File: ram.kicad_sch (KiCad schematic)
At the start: 9 parts, among them U10 HyperRAM

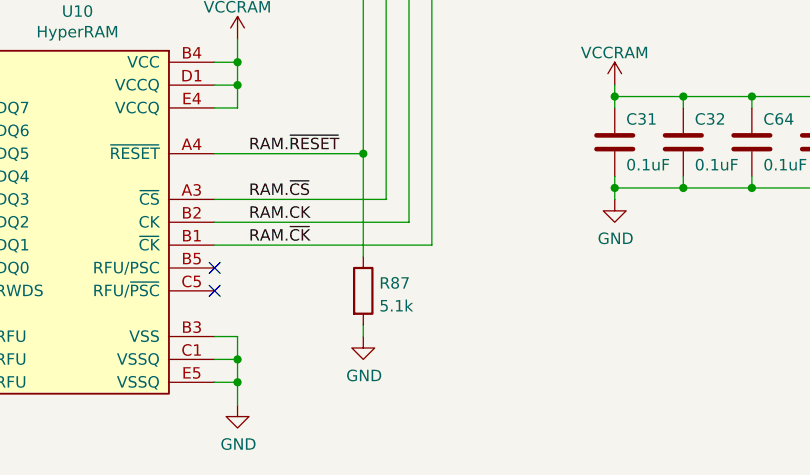
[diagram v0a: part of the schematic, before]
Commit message: add first round of hits on lcsc
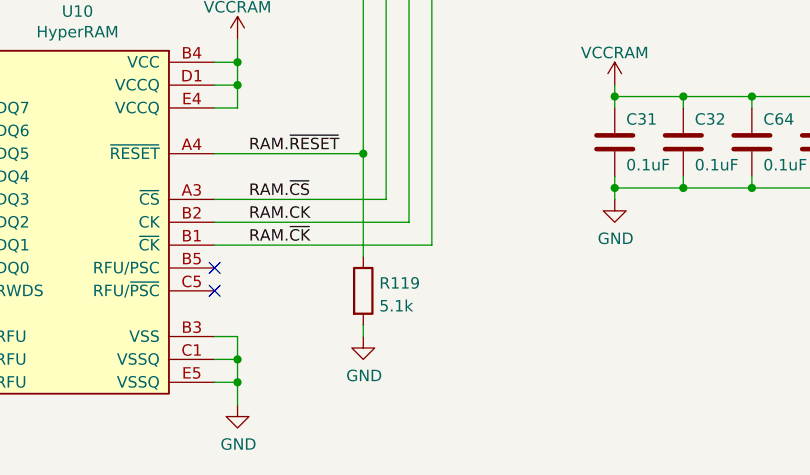
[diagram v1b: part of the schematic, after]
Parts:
- C19, C21, C5: LCSC# (none) -> C318573
- C31, C32, C64, C65: LCSC# (none) -> C100072
- R119: renamed from R87; LCSC# (none) -> C105873
